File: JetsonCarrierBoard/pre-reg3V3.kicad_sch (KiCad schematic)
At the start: 18 parts

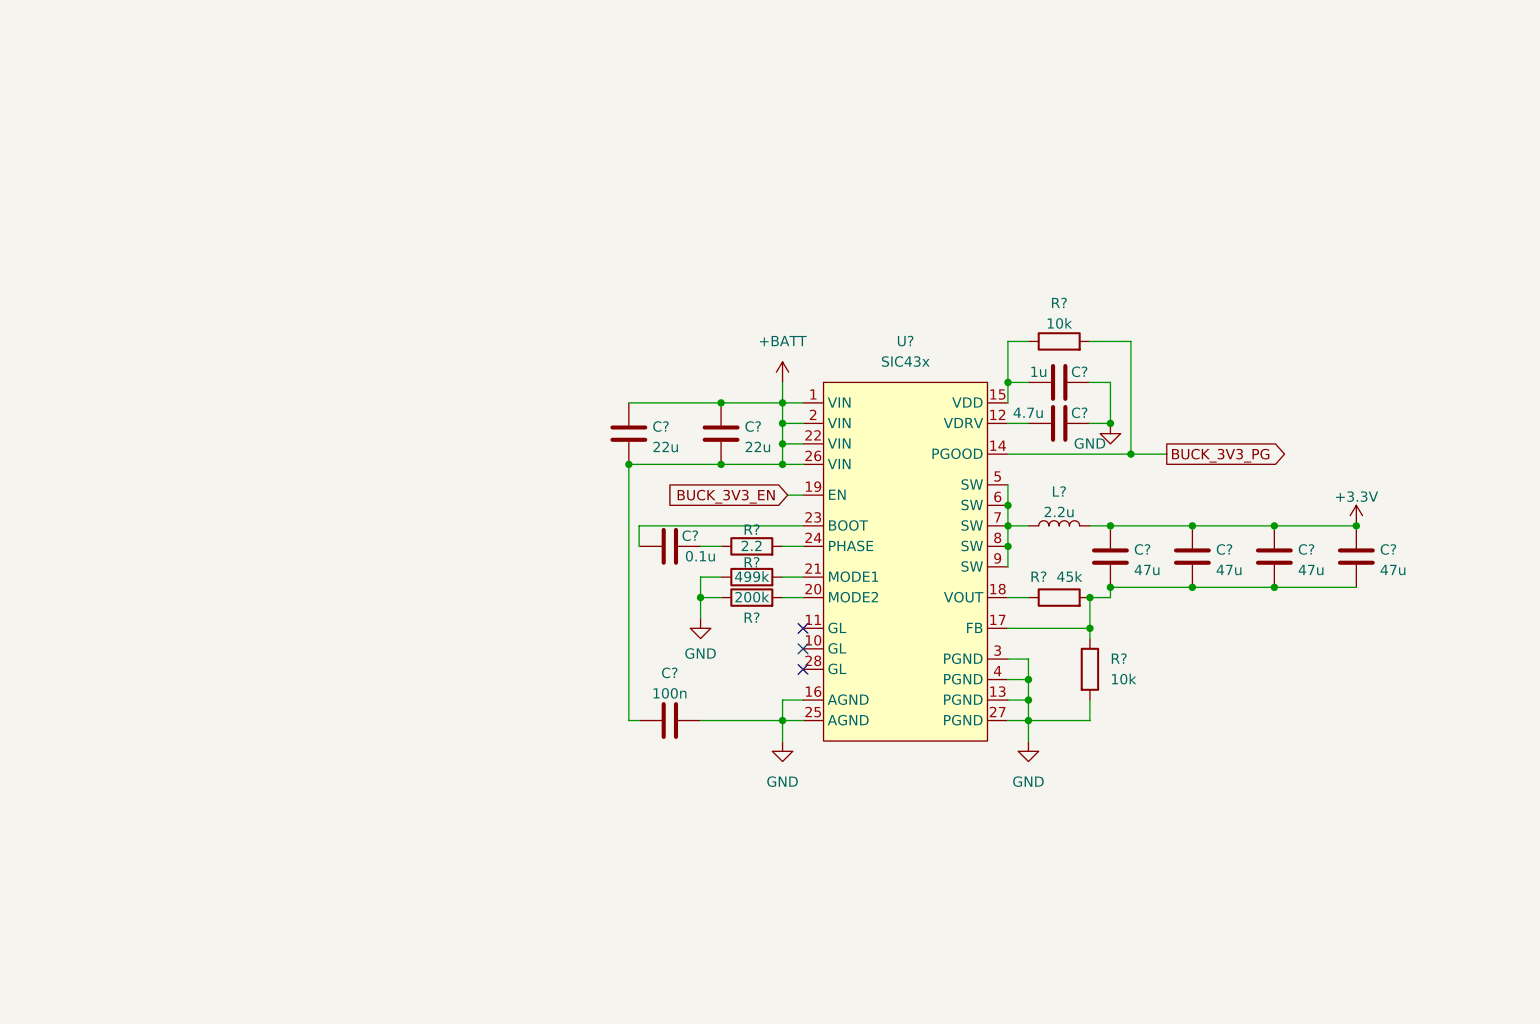
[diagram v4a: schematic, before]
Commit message: Improvement list, fixes, and readability improvements
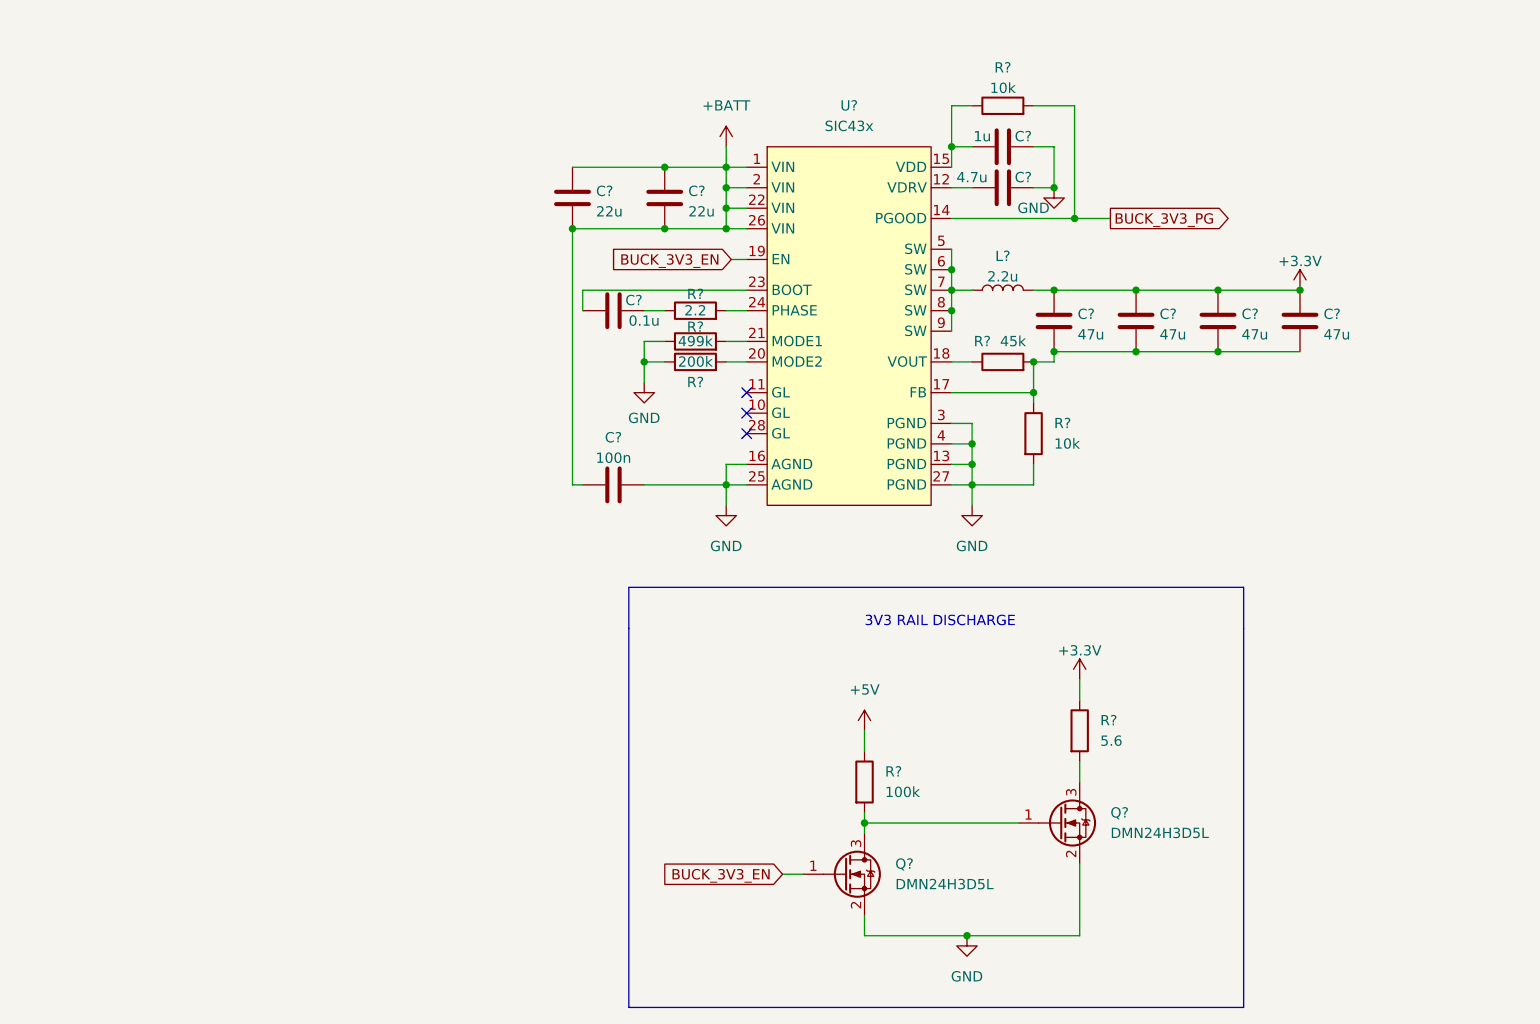
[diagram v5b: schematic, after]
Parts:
- added Q? (x2): DMN24H3D5L, Package_TO_SOT_SMD:SOT-23, symbol Transistor_FET:DMN24H3D5L
- added R?: 5.6, symbol Device:R
- added R?: 100k, symbol Device:R
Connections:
- net +3V3: now also R?.1
- net BUCK_3V3_EN: now also Q?.1 (G)
- net GND: now also Q?.2 (S), Q?.2 (S)
- new net: Q?.1 (G), Q?.3 (D), R?.2
- new net: Q?.3 (D), R?.2
- new net +5V: R?.1
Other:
- note added: "3V3 RAIL DISCHARGE"
- moved on the sheet: C?, L?, R?, U?
